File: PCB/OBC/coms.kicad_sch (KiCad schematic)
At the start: 25 parts, among them U2 STM32F405RGTx

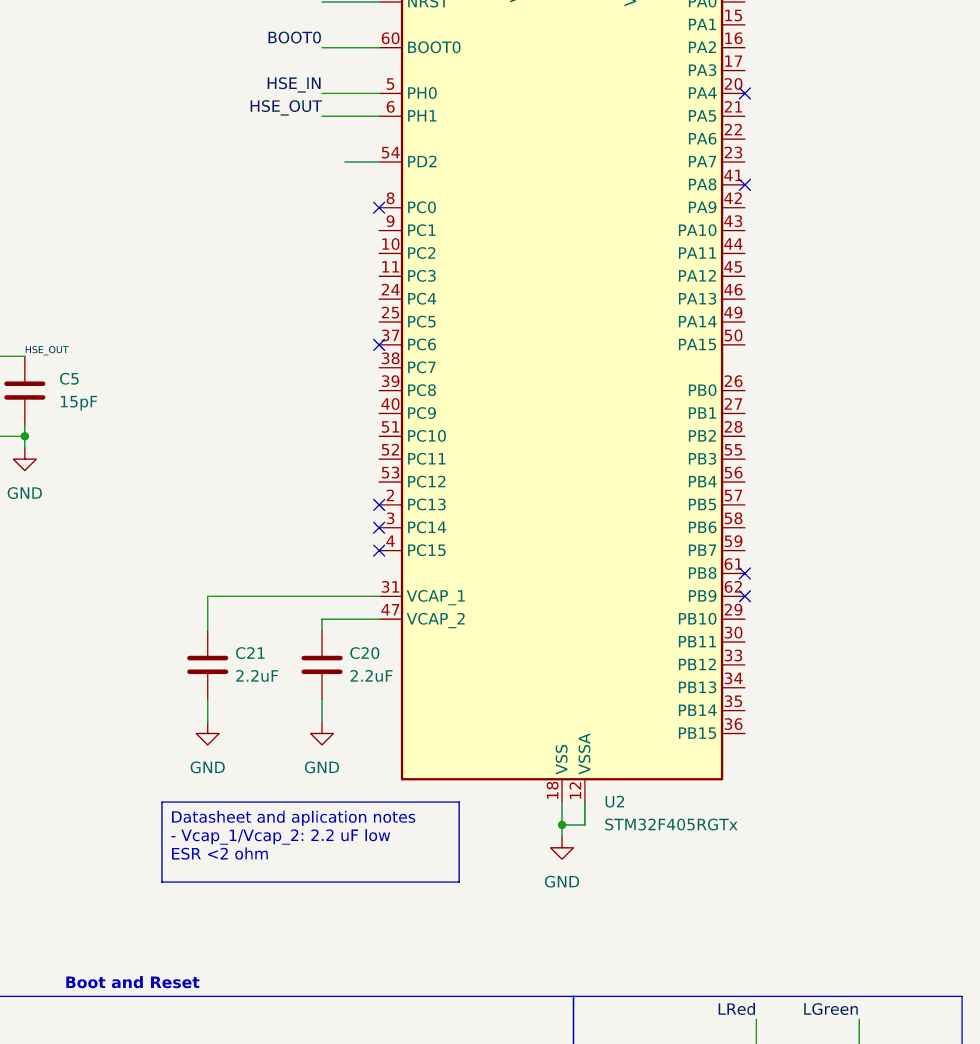
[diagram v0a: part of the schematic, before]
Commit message: Add: flash memory and mux at libraries
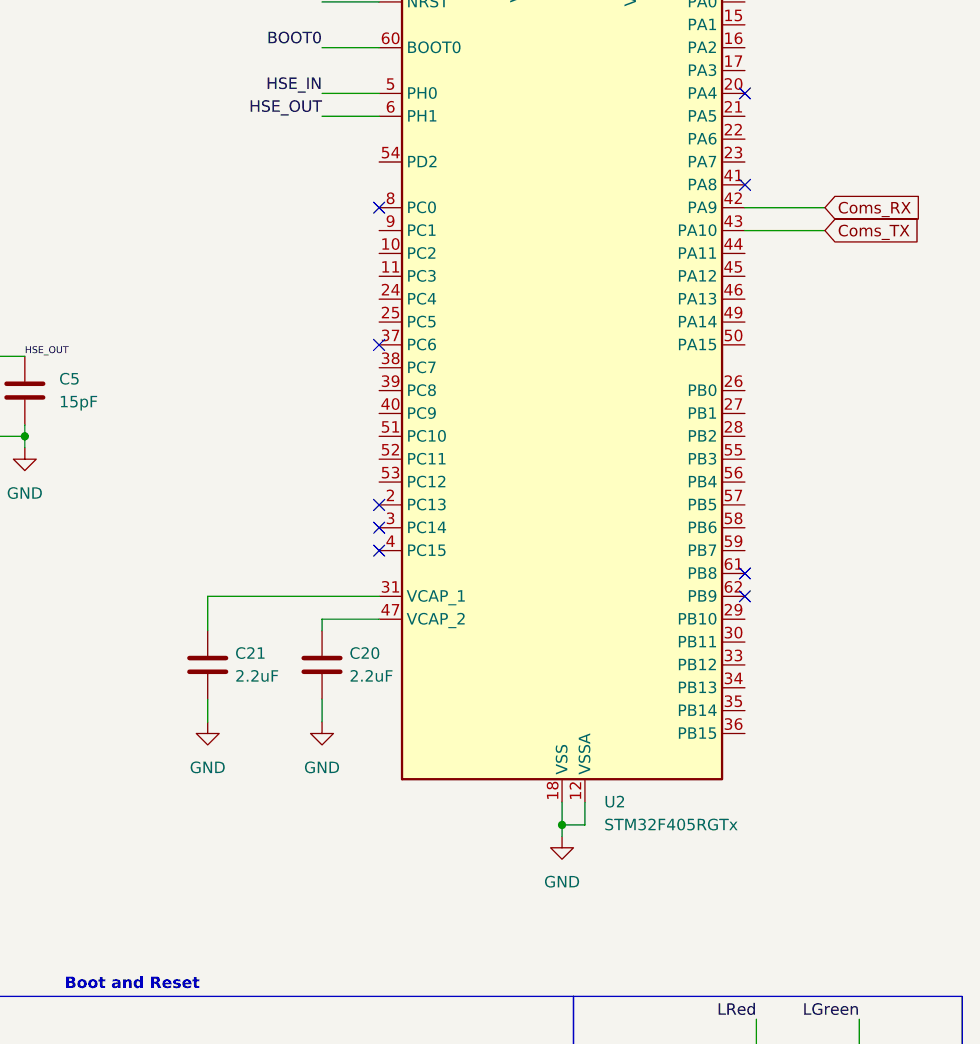
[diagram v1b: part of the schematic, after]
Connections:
- net Coms_RX: now reaches U2.42 (PA9)
- net Coms_TX: now reaches U2.43 (PA10)
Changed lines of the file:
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@@
-		)
-	)
-	(text_box "Datasheet and aplication notes\n- Vcap_1/Vcap_2: 2.2 uF low ESR <2 ohm"
-		(exclude_from_sim no)
-		(at 80.01 137.16 0)
-		(size 33.02 8.89)
-		(margins 0.9525 0.9525 0.9525 0.9525)
-		(stroke
-			(width 0)
-			(type solid)
-		)
-		(fill
-			(type none)
-		)
-		(effects
-			(font
-				(size 1.27 1.27)
-			)
-			(justify left top)
 		)
 	)
@@
 	(wire
 		(pts
+			(xy 144.78 71.12) (xy 153.67 71.12)
+		)
+		(stroke
+			(width 0)
+			(type default)
+		)
+	)
+	(wire
+		(pts
 			(xy 129.54 40.64) (xy 129.54 39.37)
 		)
@@
 	(wire
 		(pts
+			(xy 144.78 73.66) (xy 153.67 73.66)
+		)
+		(stroke
+			(width 0)
+			(type default)
+		)
+	)
+	(wire
+		(pts
 			(xy 132.08 31.75) (xy 148.59 31.75)
 		)
@@
 		(pts
 			(xy 85.09 40.64) (xy 73.66 40.64)
-		)
-		(stroke
-			(width 0)
-			(type default)
-		)
-	)
-	(wire
-		(pts
-			(xy 100.33 66.04) (xy 104.14 66.04)
 		)
 		(stroke
@@
 			)
 			(justify right bottom)
+		)
+	)
+	(global_label "Coms_TX"
+		(shape input)
+		(at 153.67 73.66 0)
+		(fields_autoplaced yes)
+		(effects
+			(font
+				(size 1.27 1.27)
+			)
+			(justify left)
+		)
+		(property "Intersheetrefs" "${INTERSHEET_REFS}"
+			(at 164.9403 73.66 0)
+			(effects
+				(font
+					(size 1.27 1.27)
+				)
+				(justify left)
+				(hide yes)
+			)
 		)
 	)
@@
 				(hide yes)
 			)
+		)
+	)
+	(global_label "Coms_RX"
+		(shape input)
+		(at 153.67 71.12 0)
+		(fields_autoplaced yes)
+		(effects
+			(font
+				(size 1.27 1.27)
+			)
+			(justify left)
+		)
+		(property "Intersheetrefs" "${INTERSHEET_REFS}"
+			(at 165.2427 71.12 0)
+			(effects
+				(font
+					(size 1.27 1.27)
+				)
+				(justify left)
+				(hide yes)
+			)

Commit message: Watchdog
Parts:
- added C3, C9: 100nF, symbol Device:C
- added C4: 1uF, symbol Device:C
- added R1, R2: 10k, symbol Device:R
- added U1: W25Q128JVSIQ, SOIC_128JVSIQ_WIN, symbol W25Q128JVSIQ:W25Q128JVSIQ
- added U4: TMUX1574PWR, PWP16_2P31X2P46_TEX, symbol TMUX1574PWR:TMUX1574PWR
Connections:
- net +3V3: now also C3.1, C4.1, C9.1, R1.1, R2.2, U1.8 (VCC), U4.16 (VDD)
- net GND: now also C3.2, C4.2, C9.2, U1.1 (/CS), U1.4 (GND), U4.15 (*EN), U4.8 (GND)
- new net: R1.2, U1.7 (/HOLD_or_/RESET_(IO3))
- new net: R2.1, U1.3
- new net coms_flash_clk_m: U1.6 (CLK), U4.12 (D4)
- new net coms_flash_miso_m: U1.2 (DO_(IO1)), U4.7 (D2)
- new net coms_flash_mosi_m: U1.5 (DI_(IO0)), U4.9 (D3)
- new net select_coms: U4.1 (SEL)
- no-connect marks 9 -> 10
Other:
- note added: "100nF: X5R o X7R, minimo 16V, 0805"
- moved on the sheet: C1, C2, C20, C21, C22, C23, C24, C25, C26, C27, C28, C29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

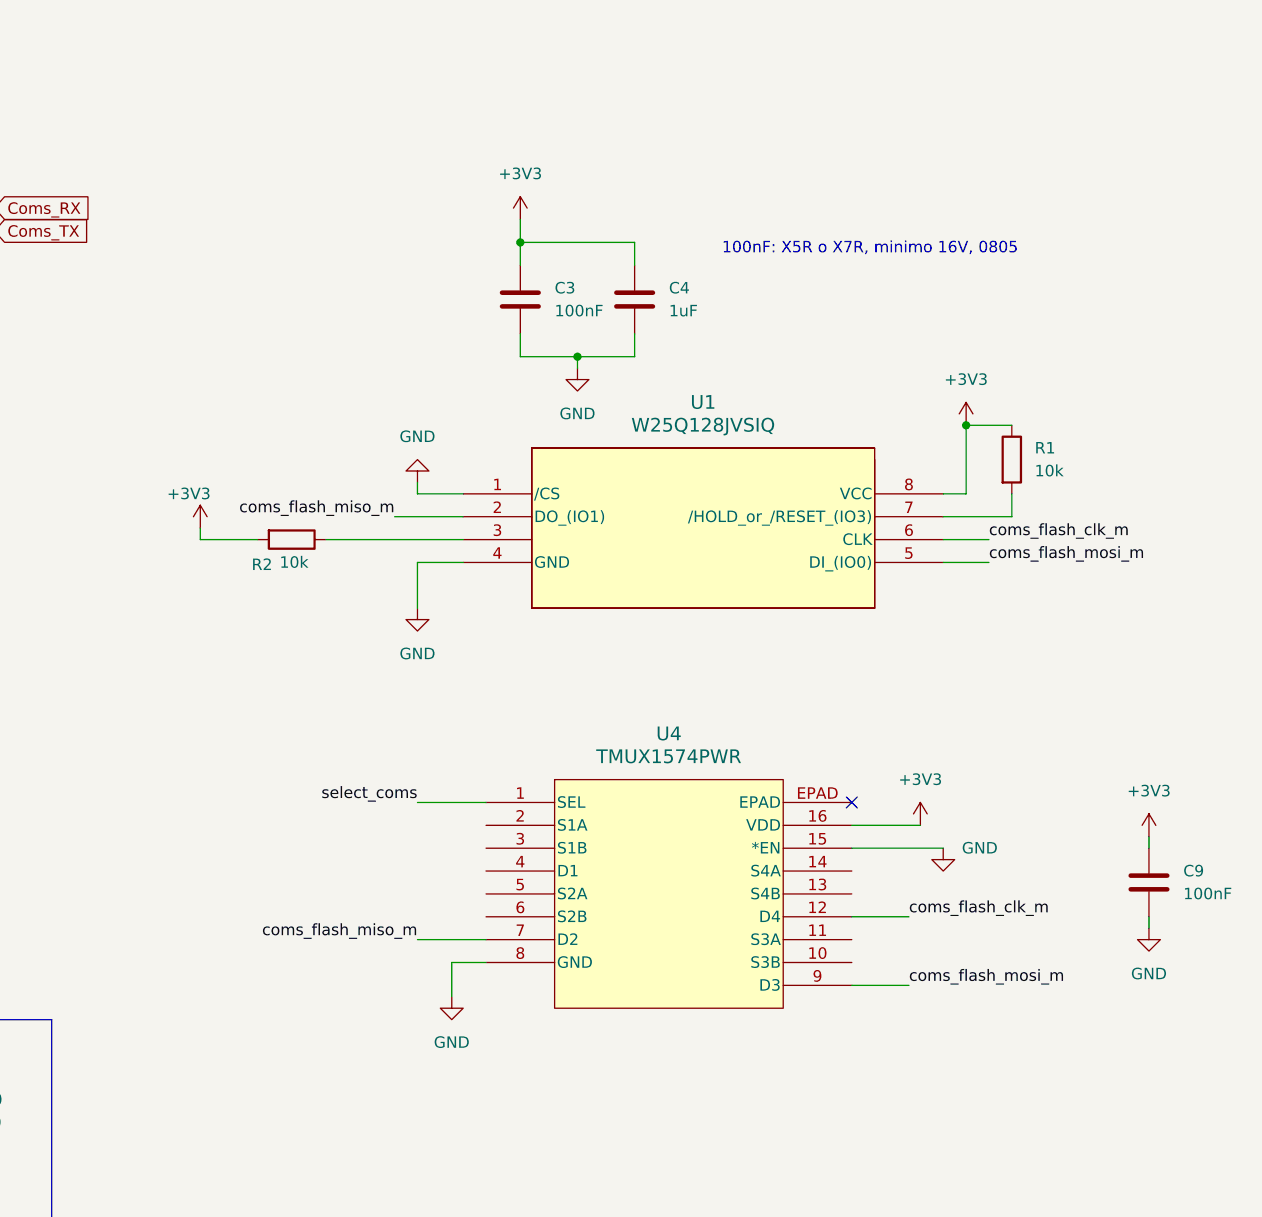
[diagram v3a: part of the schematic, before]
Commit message: Add: Can bus
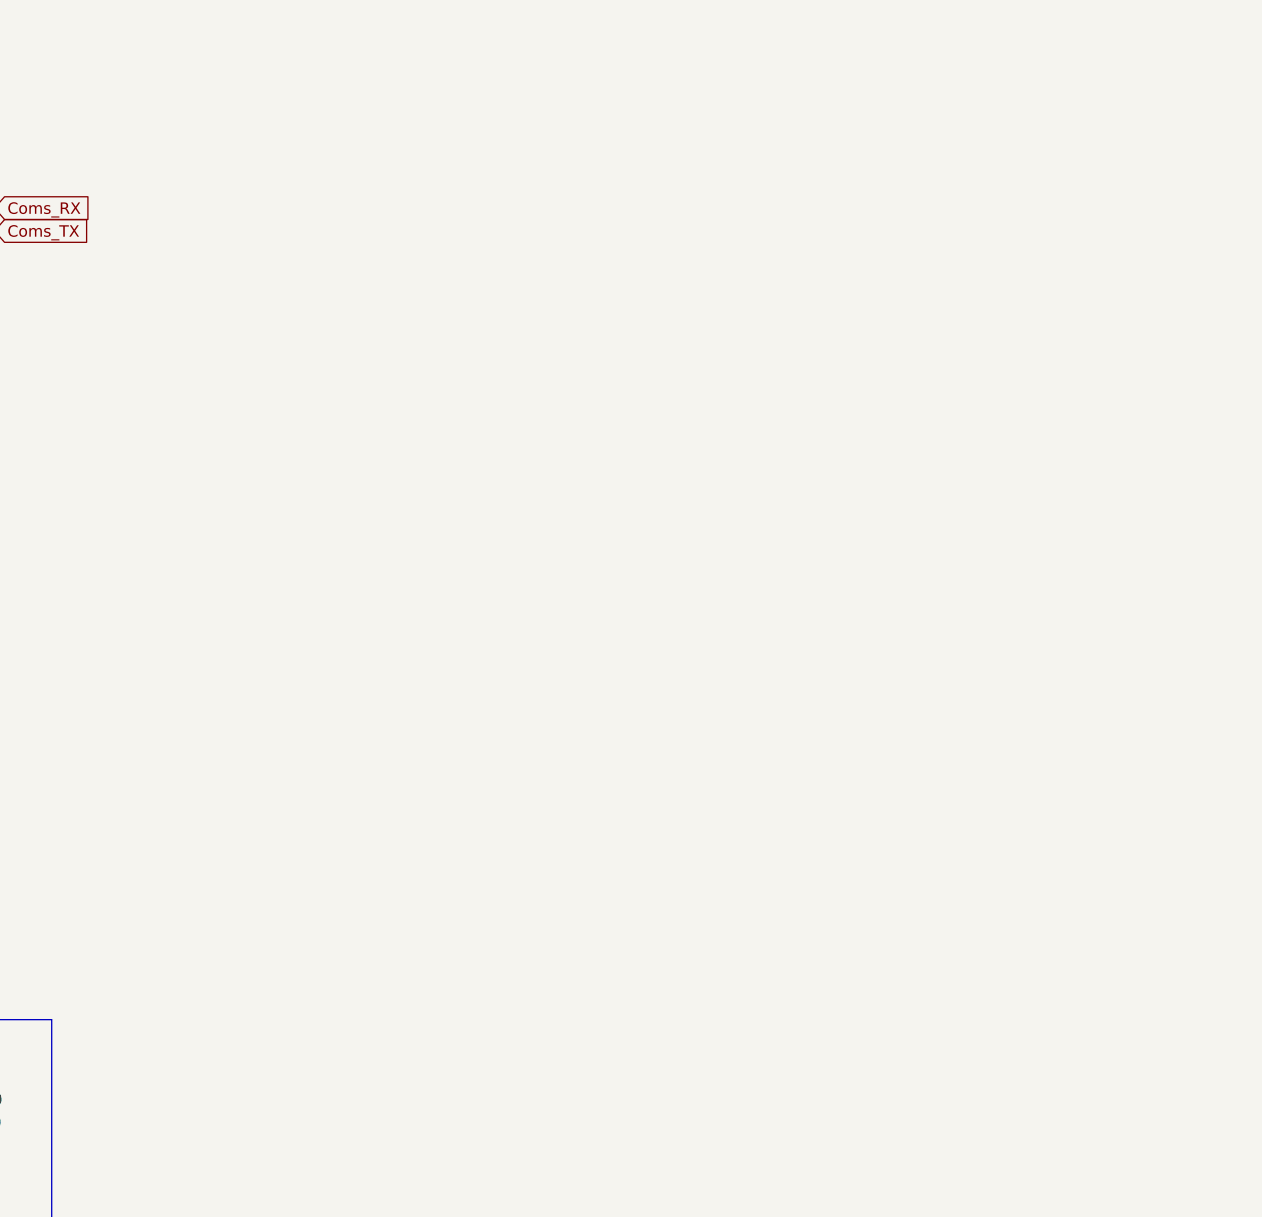
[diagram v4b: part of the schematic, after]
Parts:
- removed C3, C9: 100nF, symbol Device:C
- removed C4: 1uF, symbol Device:C
- removed R1, R2: 10k, symbol Device:R
- removed U1: W25Q128JVSIQ, SOIC_128JVSIQ_WIN, symbol W25Q128JVSIQ:W25Q128JVSIQ
- removed U4: TMUX1574PWR, PWP16_2P31X2P46_TEX, symbol TMUX1574PWR:TMUX1574PWR
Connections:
- no-connect marks 10 -> 9
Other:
- note removed: "100nF: X5R o X7R, minimo 16V, 0805"

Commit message: minors changes
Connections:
- net SWDIO1: now reaches U2.46 (PA13)
- net SWCLK1: now reaches U2.49 (PA14)
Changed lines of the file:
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@@
 	(wire
 		(pts
-			(xy 137.16 71.12) (xy 146.05 71.12)
+			(xy 137.16 71.12) (xy 143.51 71.12)
 		)
 		(stroke
@@
 	(wire
 		(pts
-			(xy 137.16 73.66) (xy 146.05 73.66)
+			(xy 137.16 73.66) (xy 143.51 73.66)
 		)
 		(stroke
@@
 	(wire
 		(pts
+			(xy 137.16 81.28) (xy 143.51 81.28)
+		)
+		(stroke
+			(width 0)
+			(type default)
+		)
+	)
+	(wire
+		(pts
 			(xy 116.84 139.7) (xy 116.84 137.16)
 		)
@@
 		(pts
 			(xy 119.38 139.7) (xy 116.84 139.7)
+		)
+		(stroke
+			(width 0)
+			(type default)
+		)
+	)
+	(wire
+		(pts
+			(xy 137.16 83.82) (xy 143.51 83.82)
 		)
 		(stroke
@@
 		)
 	)
+	(global_label "SWCLK1"
+		(shape input)
+		(at 143.51 83.82 0)
+		(fields_autoplaced yes)
+		(effects
+			(font
+				(size 1.27 1.27)
+			)
+			(justify left)
+		)
+		(property "Intersheetrefs" "${INTERSHEET_REFS}"
+			(at 153.9337 83.82 0)
+			(effects
+				(font
+					(size 1.27 1.27)
+				)
+				(justify left)
+				(hide yes)
+			)
+		)
+	)
 	(global_label "Coms_TX"
 		(shape input)
-		(at 146.05 73.66 0)
+		(at 143.51 73.66 0)
 		(fields_autoplaced yes)
 		(effects
@@
 		)
 		(property "Intersheetrefs" "${INTERSHEET_REFS}"
-			(at 157.3203 73.66 0)
+			(at 154.7803 73.66 0)
 			(effects
 				(font
@@
 		)
 	)
+	(global_label "SWDIO1"
+		(shape input)
+		(at 143.51 81.28 0)
+		(fields_autoplaced yes)
+		(effects
+			(font
+				(size 1.27 1.27)
+			)
+			(justify left)
+		)
+		(property "Intersheetrefs" "${INTERSHEET_REFS}"
+			(at 153.5709 81.28 0)
+			(effects
+				(font
+					(size 1.27 1.27)
+				)
+				(justify left)
+				(hide yes)
+			)
+		)
+	)
 	(global_label "Coms_RX"
 		(shape input)
-		(at 146.05 71.12 0)
+		(at 143.51 71.12 0)
 		(fields_autoplaced yes)
 		(effects
@@
 		)
 		(property "Intersheetrefs" "${INTERSHEET_REFS}"
-			(at 157.6227 71.12 0)
+			(at 155.0827 71.12 0)
 			(effects
 				(font

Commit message: cambiode OCP
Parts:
- XTAL2: renamed from XTAL1; footprint ESCMHZ:ECS-80-12_ECS -> ECS-80-12-30BQ-JES-TR:ECS-80-12_ECS
- renumbered C28 to C18, C6 to C19, C27 to C20, C1 to C21, C26 to C22, C2 to C23, C25 to C24, C5 to C25, C24 to C26, C23 to C27, C21 to C28, C20 to C29, C32 to C30, C22 to C31, C29 to C32, D8 to D4, D7 to D5, R20 to R10, R14 to R8, R19 to R9, SwBoot1 to SwBoot2, SwReset1 to SwReset2, U2 to U4

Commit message: New
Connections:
- net SWCLK1 renamed SWCLK2
- net SWDIO1 renamed SWDIO2
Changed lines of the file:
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@@
 		)
 	)
-	(global_label "SWCLK1"
+	(global_label "SWCLK2"
 		(shape input)
 		(at 143.51 83.82 0)
@@
 		)
 	)
-	(global_label "SWDIO1"
+	(global_label "SWDIO2"
 		(shape input)
 		(at 143.51 81.28 0)
